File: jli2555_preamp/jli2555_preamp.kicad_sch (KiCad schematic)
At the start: 25 parts, among them Q2 J113, U1 NMA0515SC, U2 NE5532

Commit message: Finalize inital design of schematic
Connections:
- net -15V: now also C6.2; no longer C6.1
- net GND: now also C6.1; no longer C6.2
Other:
- moved on the sheet: C6
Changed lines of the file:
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@@
 	(symbol
 		(lib_id "Device:C_Polarized")
-		(at 156.21 129.54 0)
-		(mirror y)
+		(at 156.21 129.54 180)
 		(unit 1)
 		(exclude_from_sim no)
@@
 		(on_board yes)
 		(dnp no)
-		(fields_autoplaced yes)
 		(property "Reference" "C6"
-			(at 160.02 127.3809 0)
+			(at 160.02 131.6991 0)
 			(effects
 				(font
@@
 		)
 		(property "Value" "2200u"
-			(at 160.02 129.9209 0)
+			(at 160.02 129.1591 0)
 			(effects
 				(font
@@
 		)
 		(property "Footprint" ""
-			(at 155.2448 133.35 0)
+			(at 155.2448 125.73 0)
 			(effects
 				(font

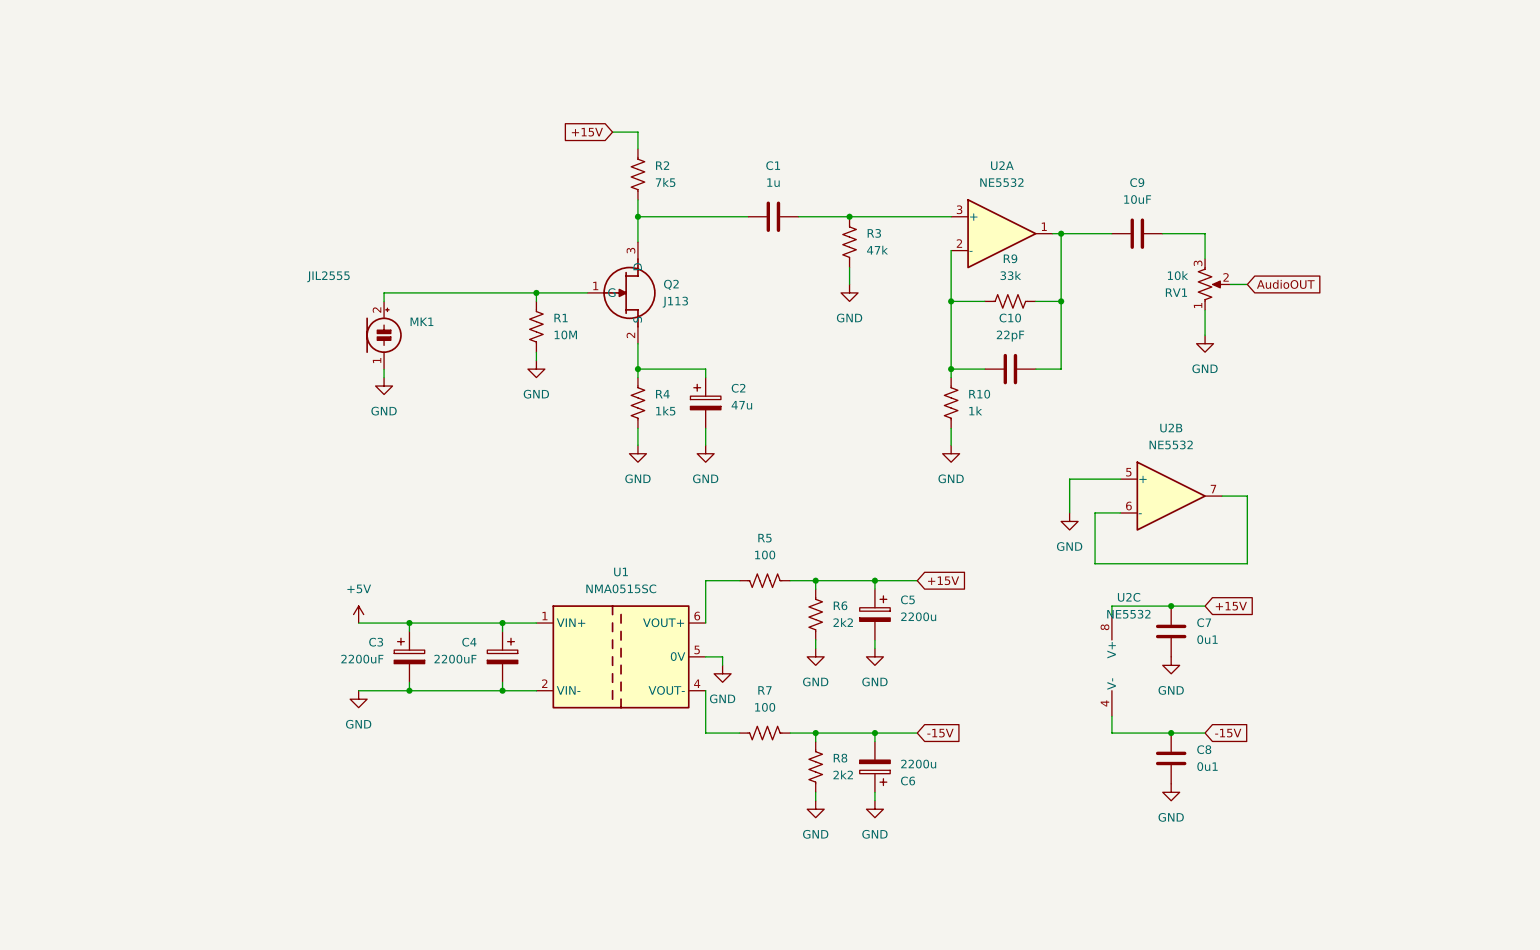
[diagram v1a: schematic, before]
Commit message: Last version using USB power, JFET to op amp change
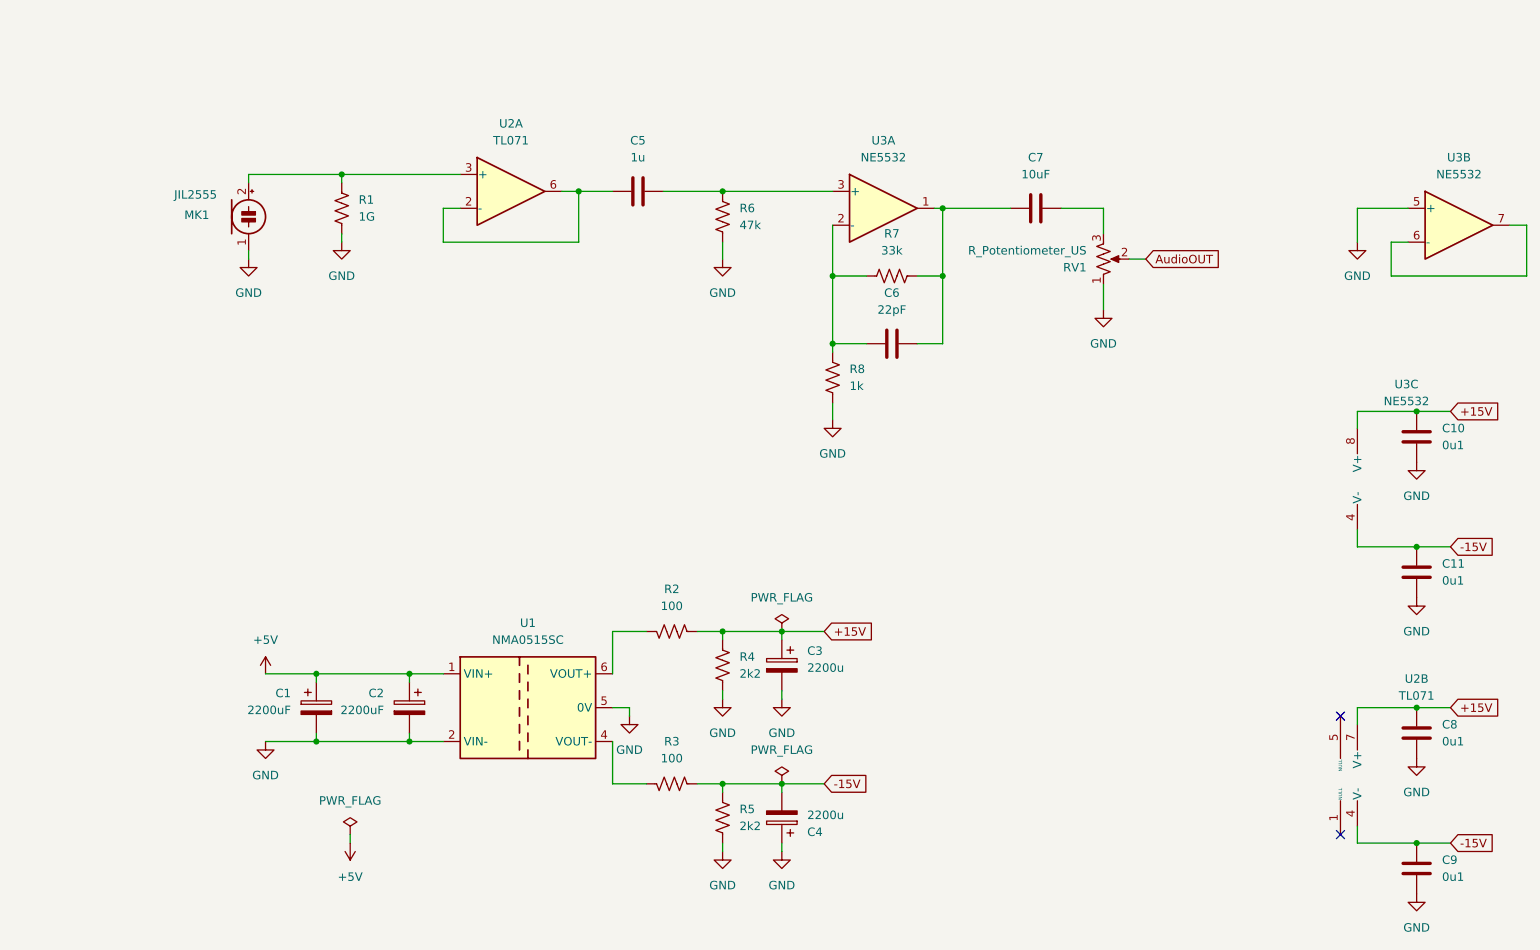
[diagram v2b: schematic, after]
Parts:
- removed C2: 47u, symbol Device:C_Polarized
- removed Q2: J113, J113D74Z, symbol J113-D74Z:J113-D74Z
- removed R2: 7k5, symbol Device:R_US
- removed R4: 1k5, symbol Device:R_US
- added C8, C9: 0u1, Capacitor_THT:C_Disc_D3.0mm_W1.6mm_P2.50mm, symbol Device:C
- added U2: TL071, Package_DIP:DIP-8_W7.62mm_Socket, symbol Anauseam:TL071
- C1: renamed from C3; footprint (none) -> Capacitor_THT:CP_Radial_D12.5mm_P5.00mm
- C10: renamed from C7; footprint (none) -> Capacitor_THT:C_Disc_D3.0mm_W1.6mm_P2.50mm
- C11: renamed from C8; footprint (none) -> Capacitor_THT:C_Disc_D3.0mm_W1.6mm_P2.50mm
- C2: renamed from C4; footprint (none) -> Capacitor_THT:CP_Radial_D12.5mm_P5.00mm
- C3: renamed from C5; footprint (none) -> Capacitor_THT:CP_Radial_D12.5mm_P5.00mm
- C4: renamed from C6; footprint (none) -> Capacitor_THT:CP_Radial_D12.5mm_P5.00mm
- C5: renamed from C1; footprint (none) -> Capacitor_THT:C_Rect_L7.0mm_W4.5mm_P5.00mm
- C6: renamed from C10; footprint (none) -> Capacitor_THT:C_Disc_D4.3mm_W1.9mm_P5.00mm
- C7: renamed from C9; footprint (none) -> Capacitor_THT:CP_Radial_D5.0mm_P2.50mm
- MK1: footprint (none) -> Connector_Wire:SolderWire-0.1sqmm_1x02_P3.6mm_D0.4mm_OD1mm
- R1: value 10M -> 1G; footprint (none) -> Resistor_THT:R_Axial_DIN0207_L6.3mm_D2.5mm_P7.62mm_Horizontal
- R2: renamed from R5; footprint (none) -> Resistor_THT:R_Axial_DIN0207_L6.3mm_D2.5mm_P7.62mm_Horizontal
- R3: renamed from R7; footprint (none) -> Resistor_THT:R_Axial_DIN0207_L6.3mm_D2.5mm_P7.62mm_Horizontal
- R4: renamed from R6; footprint (none) -> Resistor_THT:R_Axial_DIN0207_L6.3mm_D2.5mm_P7.62mm_Horizontal
- R5: renamed from R8; footprint (none) -> Resistor_THT:R_Axial_DIN0207_L6.3mm_D2.5mm_P7.62mm_Horizontal
- R6: renamed from R3; footprint (none) -> Resistor_THT:R_Axial_DIN0207_L6.3mm_D2.5mm_P7.62mm_Horizontal
- R7: renamed from R9; footprint (none) -> Resistor_THT:R_Axial_DIN0207_L6.3mm_D2.5mm_P7.62mm_Horizontal
- R8: renamed from R10; footprint (none) -> Resistor_THT:R_Axial_DIN0207_L6.3mm_D2.5mm_P7.62mm_Horizontal
- RV1: value 10k -> R_Potentiometer_US; footprint (none) -> Potentiometer_THT:Potentiometer_Alps_RK09Y11_Single_Horizontal
- U3: renamed from U2; footprint (none) -> Package_DIP:DIP-8_W7.62mm_Socket
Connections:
- net +15V: now also C8.2, U2.7 (V+)
- net -15V: now also C9.2, U2.4 (V-)
- net GND: now also C8.1, C9.1
- net at MK1.2 (+), R1.1: now also U2.3 (+)
- net at C5.1: now also U2.2 (-), U2.6
- no-connect marks 0 -> 2
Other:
- moved on the sheet: C1, C10, C11, C2, C3, C4, C5, C6, C7, MK1, R1, R2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

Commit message: Overhaul of the power supply, will now be a 9v supply for greater simplicity
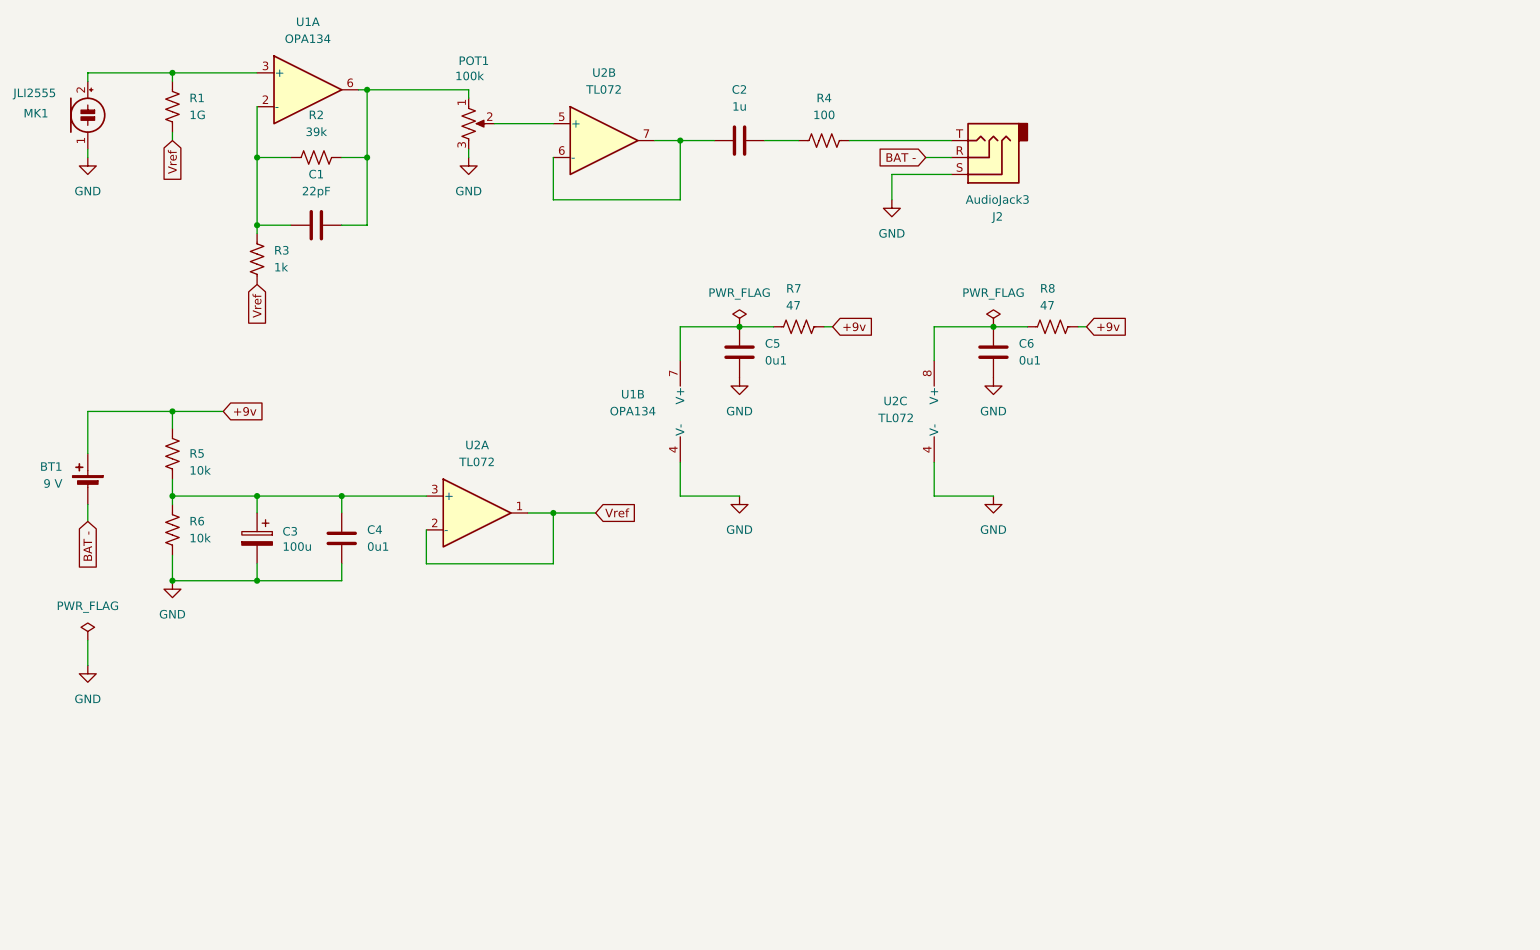
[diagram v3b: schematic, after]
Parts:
- removed C1, C2: 2200uF, Capacitor_THT:CP_Radial_D12.5mm_P5.00mm, symbol Device:C_Polarized
- removed C10, C11, C9: 0u1, Capacitor_THT:C_Disc_D3.0mm_W1.6mm_P2.50mm, symbol Device:C
- removed C4: 2200u, Capacitor_THT:CP_Radial_D12.5mm_P5.00mm, symbol Device:C_Polarized
- removed C7: 10uF, Capacitor_THT:CP_Radial_D5.0mm_P2.50mm, symbol Device:C
- removed U1: NMA0515SC, Converter_DCDC:Converter_DCDC_Murata_NMAxxxxSC_THT, symbol Regulator_Switching:NMA0515SC
- removed U2: TL071, Package_DIP:DIP-8_W7.62mm_Socket, symbol Anauseam:TL071
- removed U3: NE5532, Package_DIP:DIP-8_W7.62mm_Socket, symbol Amplifier_Operational:NE5532
- added BT1: 9 V, Battery:BatteryHolder_MPD_BA9VPC_1xPP3, symbol Device:Battery_Cell
- added C1: 22pF, Capacitor_THT:C_Disc_D5.0mm_W2.5mm_P2.50mm, symbol Device:C
- added C4: 0u1, Capacitor_THT:C_Disc_D5.0mm_W2.5mm_P5.00mm, symbol Device:C
- added J2: AudioJack3, Connector_Audio:Jack_3.5mm_CUI_SJ1-3513N_Horizontal, symbol Connector_Audio:AudioJack3
- added U1: OPA134, Package_DIP:DIP-8_W7.62mm_Socket, symbol Anauseam:OPA134
- added U2: TL072, Package_DIP:DIP-8_W7.62mm_Socket, symbol Amplifier_Operational:TL072
- C2: renamed from C5; footprint Capacitor_THT:C_Rect_L7.0mm_W4.5mm_P5.00mm -> Capacitor_THT:C_Rect_L7.2mm_W4.5mm_P5.00mm_FKS2_FKP2_MKS2_MKP2
- C3: value 2200u -> 100u; footprint Capacitor_THT:CP_Radial_D12.5mm_P5.00mm -> Capacitor_THT:CP_Radial_D6.3mm_P2.50mm
- C5: renamed from C8; footprint Capacitor_THT:C_Disc_D3.0mm_W1.6mm_P2.50mm -> Capacitor_THT:C_Disc_D5.0mm_W2.5mm_P2.50mm
- C6: value 22pF -> 0u1; footprint Capacitor_THT:C_Disc_D4.3mm_W1.9mm_P5.00mm -> Capacitor_THT:C_Disc_D5.0mm_W2.5mm_P2.50mm
- MK1: value JIL2555 -> JLI2555
- POT1: renamed from RV1; value R_Potentiometer_US -> 100k
- R1: footprint Resistor_THT:R_Axial_DIN0207_L6.3mm_D2.5mm_P7.62mm_Horizontal -> Resistor_THT:R_Axial_DIN0207_L6.3mm_D2.5mm_P10.16mm_Horizontal
- R2: value 100 -> 39k; footprint Resistor_THT:R_Axial_DIN0207_L6.3mm_D2.5mm_P7.62mm_Horizontal -> Resistor_THT:R_Axial_DIN0207_L6.3mm_D2.5mm_P10.16mm_Horizontal
- R3: value 100 -> 1k; footprint Resistor_THT:R_Axial_DIN0207_L6.3mm_D2.5mm_P7.62mm_Horizontal -> Resistor_THT:R_Axial_DIN0207_L6.3mm_D2.5mm_P10.16mm_Horizontal
- R4: value 2k2 -> 100; footprint Resistor_THT:R_Axial_DIN0207_L6.3mm_D2.5mm_P7.62mm_Horizontal -> Resistor_THT:R_Axial_DIN0207_L6.3mm_D2.5mm_P10.16mm_Horizontal
- R5: value 2k2 -> 10k; footprint Resistor_THT:R_Axial_DIN0207_L6.3mm_D2.5mm_P7.62mm_Horizontal -> Resistor_THT:R_Axial_DIN0207_L6.3mm_D2.5mm_P10.16mm_Horizontal
- R6: value 47k -> 10k; footprint Resistor_THT:R_Axial_DIN0207_L6.3mm_D2.5mm_P7.62mm_Horizontal -> Resistor_THT:R_Axial_DIN0207_L6.3mm_D2.5mm_P10.16mm_Horizontal
- R7: value 33k -> 47; footprint Resistor_THT:R_Axial_DIN0207_L6.3mm_D2.5mm_P7.62mm_Horizontal -> Resistor_THT:R_Axial_DIN0207_L6.3mm_D2.5mm_P10.16mm_Horizontal
- R8: value 1k -> 47; footprint Resistor_THT:R_Axial_DIN0207_L6.3mm_D2.5mm_P7.62mm_Horizontal -> Resistor_THT:R_Axial_DIN0207_L6.3mm_D2.5mm_P10.16mm_Horizontal
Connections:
- net GND: now also C6.1, POT1.3, C4.1, J2.S, U1.4 (V-), U2.4 (V-); no longer POT1.1, R1.2, R4.2, R5.2, R8.2
- net at C2.1: now also U2.6 (-), U2.7
- net at MK1.2 (+), R1.1: now also U1.3 (+)
- net at C6.2: now also R8.1, U2.8 (V+); no longer R7.2
- net at C2.2: now also R4.1; no longer R6.1
- net at R2.2: now also POT1.1, C1.2, U1.6
- net Vref: now reaches R3.2
- net Vref: now also R1.2, U2.1, U2.2 (-)
- removed net +15V: C3.1, C5.2, R2.1, R4.1
- net -15V: no longer names the net of R3.1
- net -15V: now also R2.1, C1.1, U1.2 (-); no longer R5.1
- net AudioOUT: no longer names the net of POT1.2
- net AudioOUT: now also U2.5 (+)
- new net: J2.T, R4.2
- new net: C3.1, C4.2, R5.2, R6.1, U2.3 (+)
- new net: C5.2, R7.1, U1.7 (V+)
- new net +9v: BT1.1 (+), R5.1, R7.2, R8.2
- new net BAT -: BT1.2 (-), J2.R
- no-connect marks 2 -> 0
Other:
- title: JIL 2555 Pre-Amplifier -> JLI 2555 tin can mic 
- moved on the sheet: C2, C5, MK1, POT1, R1
